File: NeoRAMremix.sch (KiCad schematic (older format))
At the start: 27 parts, among them P1 C64-Exp-Port, Q1 2N3904, SW1 Reset, U1 HM628512BFP-5, U2 HM628512BFP-5, U3 HM628512BFP-5, U4 HM628512BFP-5

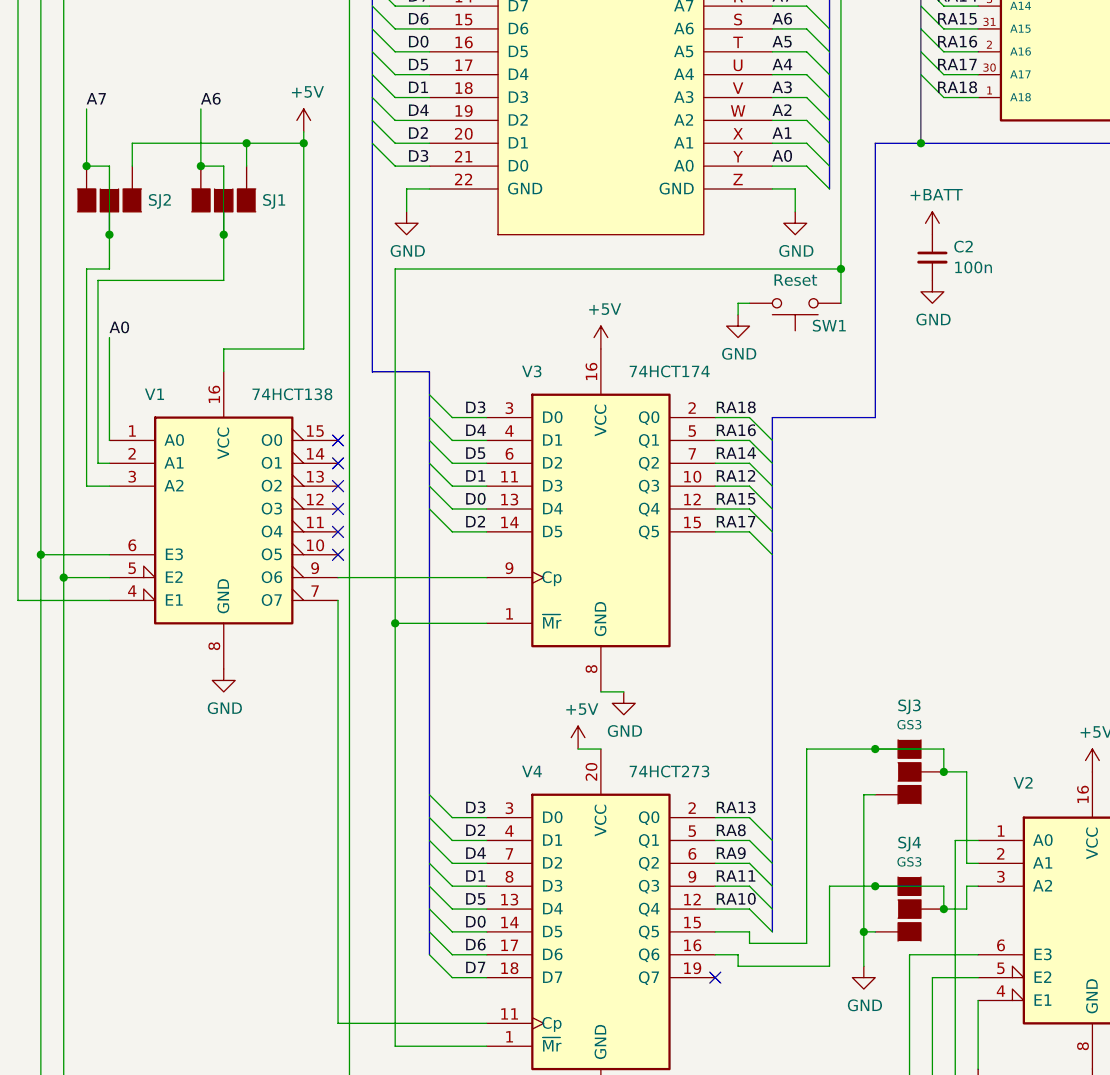
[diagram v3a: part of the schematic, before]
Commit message: Fixed solder bridges.
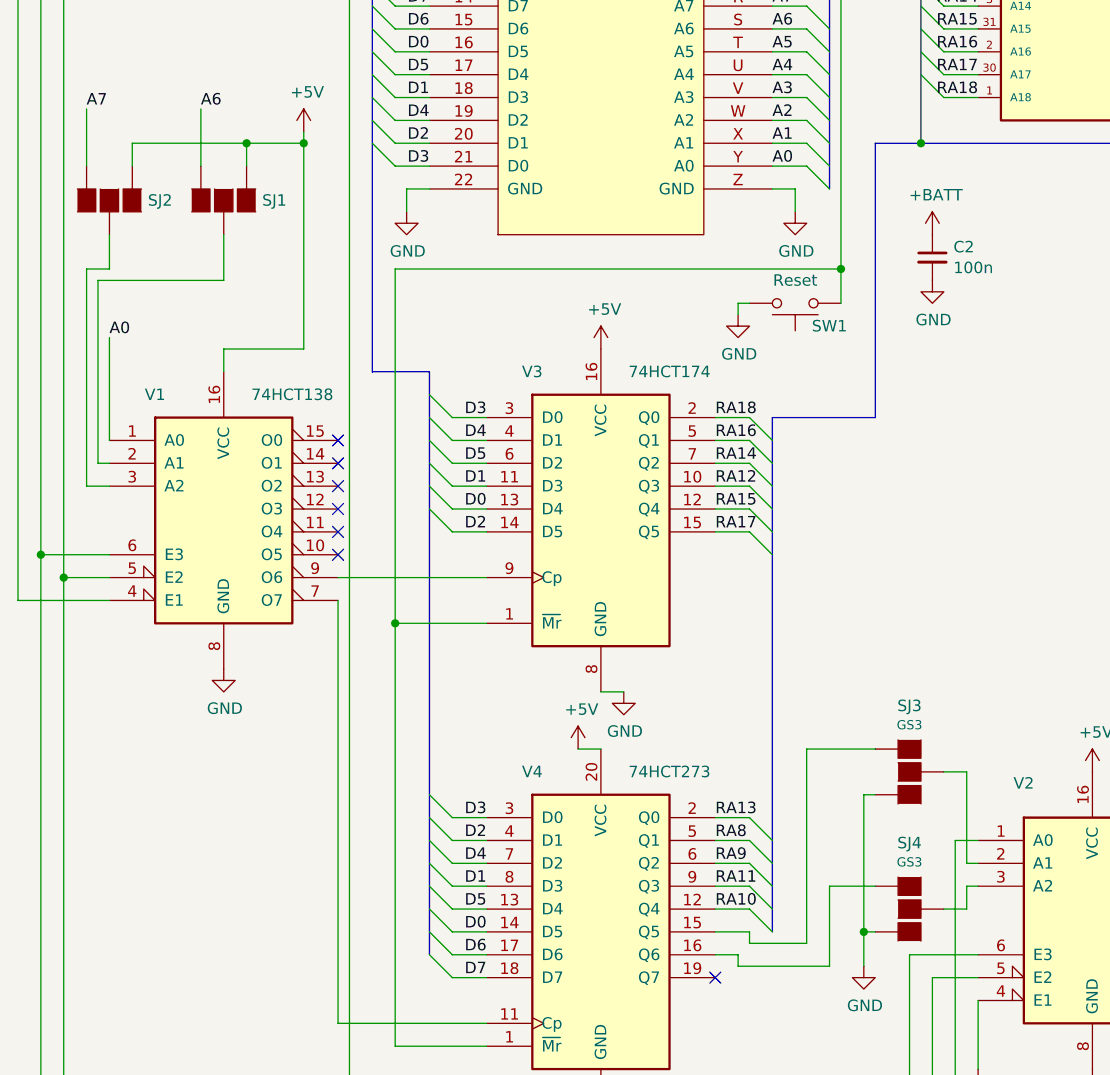
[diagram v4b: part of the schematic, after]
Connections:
- net A6: no longer SJ1.2 (G2), V1.2 (A1)
- net A7: no longer SJ2.2 (G2), V1.3 (A2)
- net at SJ3.1 (G1), V4.15 (Q5): no longer SJ3.2 (G2), V2.2 (A1)
- net at SJ4.1 (G1), V4.16 (Q6): no longer SJ4.2 (G2), V2.3 (A2)
- new net: SJ1.2 (G2), V1.2 (A1)
- new net: SJ2.2 (G2), V1.3 (A2)
- new net: SJ3.2 (G2), V2.2 (A1)
- new net: SJ4.2 (G2), V2.3 (A2)
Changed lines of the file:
@@
 	6150 3300 7850 3300
-Wire Wire Line
-	800  3400 900  3400
-Wire Wire Line
-	900  3400 900  3700
-Connection ~ 800  3400
-Connection ~ 900  3700
-Wire Wire Line
-	1300 3400 1400 3400
-Wire Wire Line
-	1400 3400 1400 3700
-Connection ~ 1300 3400
-Connection ~ 1400 3700
-Wire Wire Line
-	4250 5950 4550 5950
-Wire Wire Line
-	4550 5950 4550 6050
-Connection ~ 4250 5950
 Wire Wire Line
 	4700 6450 4650 6450
@@
 Wire Wire Line
 	4650 6050 4550 6050
-Connection ~ 4550 6050
 Wire Wire Line
 	4700 6550 4650 6550
@@
 Wire Wire Line
 	4650 6650 4550 6650
-Wire Wire Line
-	4250 6550 4550 6550
-Wire Wire Line
-	4550 6550 4550 6650
-Connection ~ 4250 6550
-Connection ~ 4550 6650
 $Comp
 L power:PWR_FLAG #FLG0103

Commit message: Fixed solder bridges.
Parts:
- removed SJ1, SJ2, SJ3, SJ4: GS3, Connectors:GS3, symbol NeoRAMremix-rescue:GS3-w_conn
- added SJ1, SJ2, SJ3, SJ4: SolderJumper_3_Bridged12, Jumper:SolderJumper-3_P1.3mm_Bridged12_RoundedPad1.0x1.5mm, symbol Jumper:SolderJumper_3_Bridged12
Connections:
- wire segments 302 -> 299
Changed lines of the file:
@@
 Wire Wire Line
 	4700 7050 4700 7350
-$Comp
-L NeoRAMremix-rescue:GS3-w_conn SJ3
-U 1 1 5C6A02C1
-P 4400 6050
-F 0 "SJ3" H 4400 6339 50  0000 C CNN
-F 1 "GS3" H 4400 6255 40  0000 C CNN
-F 2 "Connectors:GS3" H 4400 6050 50  0001 C CNN
-F 3 "" H 4400 6050 50  0001 C CNN
-	1    4400 6050
-	1    0    0    -1
-$EndComp
-$Comp
-L NeoRAMremix-rescue:GS3-w_conn SJ4
-U 1 1 5C6A0422
-P 4400 6650
-F 0 "SJ4" H 4400 6939 50  0000 C CNN
-F 1 "GS3" H 4400 6855 40  0000 C CNN
-F 2 "Connectors:GS3" H 4400 6650 50  0001 C CNN
-F 3 "" H 4400 6650 50  0001 C CNN
-	1    4400 6650
-	1    0    0    -1
-$EndComp
 NoConn ~ 3550 6950
 Wire Wire Line
@@
 	3700 6800 3950 6800
 Wire Wire Line
-	3950 6800 3950 5950
-Wire Wire Line
-	3950 5950 4250 5950
-Wire Wire Line
 	3550 6850 3650 6850
 Wire Wire Line
@@
 Wire Wire Line
 	3650 6900 4050 6900
-Wire Wire Line
-	4050 6900 4050 6550
-Wire Wire Line
-	4050 6550 4250 6550
-Wire Wire Line
-	4250 6150 4200 6150
-Wire Wire Line
-	4200 6150 4200 6750
-Wire Wire Line
-	4200 6750 4250 6750
 $Comp
 L power:GND #PWR0133
 U 1 1 5C7915DA
-P 4200 6900
-F 0 "#PWR0133" H 4200 6650 50  0001 C CNN
-F 1 "GND" H 4205 6727 50  0000 C CNN
-F 2 "" H 4200 6900 50  0001 C CNN
-F 3 "" H 4200 6900 50  0001 C CNN
-	1    4200 6900
-	1    0    0    -1
-$EndComp
-Wire Wire Line
-	4200 6750 4200 6900
-Connection ~ 4200 6750
-$Comp
-L NeoRAMremix-rescue:GS3-w_conn SJ1
-U 1 1 5C7D2316
-P 1400 3550
-F 0 "SJ1" V 1400 3718 50  0000 L CNN
-F 1 "GS3" V 1446 3718 40  0001 L CNN
-F 2 "Connectors:GS3" H 1400 3550 50  0001 C CNN
-F 3 "" H 1400 3550 50  0001 C CNN
-	1    1400 3550
-	0    1    1    0
-$EndComp
-$Comp
-L NeoRAMremix-rescue:GS3-w_conn SJ2
-U 1 1 5C7F2916
-P 900 3550
-F 0 "SJ2" V 900 3718 50  0000 L CNN
-F 1 "GS3" V 946 3718 40  0001 L CNN
-F 2 "Connectors:GS3" H 900 3550 50  0001 C CNN
-F 3 "" H 900 3550 50  0001 C CNN
-	1    900  3550
-	0    1    1    0
+P 4200 7000
+F 0 "#PWR0133" H 4200 6750 50  0001 C CNN
+F 1 "GND" H 4205 6827 50  0000 C CNN
+F 2 "" H 4200 7000 50  0001 C CNN
+F 3 "" H 4200 7000 50  0001 C CNN
+	1    4200 7000
+	1    0    0    -1
 $EndComp
 Wire Wire Line
@@
 Wire Wire Line
 	800  4800 800  3850
-Wire Wire Line
-	800  3850 900  3850
-Wire Wire Line
-	900  3850 900  3700
 $Comp
 L device:CP C1
@@
 D3
 Wire Wire Line
-	850  3900 1400 3900
-Wire Wire Line
-	1400 3900 1400 3700
-Wire Wire Line
 	850  3900 850  4700
 Wire Wire Line
 	1750 3250 1750 3300
 Wire Wire Line
-	1750 3300 1500 3300
-Wire Wire Line
-	1000 3300 1000 3400
-Wire Wire Line
-	1500 3400 1500 3300
-Connection ~ 1500 3300
-Wire Wire Line
-	1500 3300 1000 3300
-Wire Wire Line
 	1400 4300 1400 4200
 Wire Wire Line
 	1400 4200 1750 4200
 Wire Wire Line
-	1750 4200 1750 3300
+	1750 4200 1750 3550
 Connection ~ 1750 3300
-Wire Wire Line
-	800  3150 800  3400
-Wire Wire Line
-	1300 3150 1300 3400
 Text Label 6400 2100 2    50   ~ 0
 RA8
@@
 Wire Wire Line
 	4650 6050 4550 6050
-Wire Wire Line
-	4700 6550 4650 6550
-Wire Wire Line
-	4650 6550 4650 6650
-Wire Wire Line
-	4650 6650 4550 6650
 $Comp
 L power:PWR_FLAG #FLG0103
@@
 	1    0    0    -1
 $EndComp
-Text Label 1300 3150 0    50   ~ 0
+Text Label 1350 3150 0    50   ~ 0
 A6
 Text Label 800  3150 0    50   ~ 0
@@
 Wire Wire Line
 	3650 4000 3700 4000
+$Comp
+L Jumper:SolderJumper_3_Bridged12 SJ2
+U 1 1 5C5C59E5
+P 1000 3550
+F 0 "SJ2" H 1000 3664 50  0000 C CNN
+F 1 "SolderJumper_3_Bridged12" H 1000 3664 50  0001 C CNN
+F 2 "Jumper:SolderJumper-3_P1.3mm_Bridged12_RoundedPad1.0x1.5mm" H 1000 3550 50  0001 C CNN
+F 3 "~" H 1000 3550 50  0001 C CNN
+	1    1000 3550
+	1    0    0    -1
+$EndComp
+Wire Wire Line
+	800  3550 800  3150
+Wire Wire Line
+	1000 3850 1000 3700
+Wire Wire Line
+	800  3850 1000 3850
+Wire Wire Line
+	1200 3550 1200 3300
+$Comp
+L Jumper:SolderJumper_3_Bridged12 SJ1
+U 1 1 5C62F605
+P 1550 3550
+F 0 "SJ1" H 1550 3664 50  0000 C CNN
+F 1 "SolderJumper_3_Bridged12" H 1550 3664 50  0001 C CNN
+F 2 "Jumper:SolderJumper-3_P1.3mm_Bridged12_RoundedPad1.0x1.5mm" H 1550 3550 50  0001 C CNN
+F 3 "~" H 1550 3550 50  0001 C CNN
+	1    1550 3550
+	1    0    0    -1
+$EndComp
+Connection ~ 1750 3550
+Wire Wire Line
+	1750 3550 1750 3300
+Wire Wire Line
+	1200 3300 1750 3300
+Wire Wire Line
+	850  3900 1550 3900
+Wire Wire Line
+	1550 3900 1550 3700
+Wire Wire Line
+	1350 3550 1350 3150
+$Comp
+L Jumper:SolderJumper_3_Bridged12 SJ3
+U 1 1 5C6BABBB
+P 4400 6050
+F 0 "SJ3" V 4400 6118 50  0000 L CNN
+F 1 "SolderJumper_3_Bridged12" H 4400 6164 50  0001 C CNN
+F 2 "Jumper:SolderJumper-3_P1.3mm_Bridged12_RoundedPad1.0x1.5mm" H 4400 6050 50  0001 C CNN
+F 3 "~" H 4400 6050 50  0001 C CNN
+	1    4400 6050
+	0    -1   1    0
+$EndComp
+Wire Wire Line
+	3950 5850 4400 5850
+Wire Wire Line
+	3950 5850 3950 6800
+$Comp
+L Jumper:SolderJumper_3_Bridged12 SJ4
+U 1 1 5C7687C6
+P 4400 6550
+F 0 "SJ4" V 4400 6618 50  0000 L CNN
+F 1 "SolderJumper_3_Bridged12" H 4400 6664 50  0001 C CNN
+F 2 "Jumper:SolderJumper-3_P1.3mm_Bridged12_RoundedPad1.0x1.5mm" H 4400 6550 50  0001 C CNN
+F 3 "~" H 4400 6550 50  0001 C CNN
+	1    4400 6550
+	0    -1   1    0
+$EndComp
+Wire Wire Line
+	4700 6550 4550 6550
+Wire Wire Line
+	4050 6350 4400 6350
+Wire Wire Line
+	4050 6350 4050 6900
+Wire Wire Line
+	4200 6750 4200 7000
+Wire Wire Line
+	4200 6750 4400 6750
+Wire Wire Line
+	4200 6750 4200 6250
+Wire Wire Line
+	4200 6250 4400 6250
 Wire Bus Line
 	6150 2000 6150 3300
@@
 Wire Bus Line
 	2300 4300 2300 6850
+Connection ~ 4200 6750
 $EndSCHEMATC

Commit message: Fixing RAM footprint.
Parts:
- U4: footprint Housings_SSOP:TSOP-II-32_21.0x10.2mm_Pitch1.27mm -> NeoRAMremix:SO32_FP32D_20.45x11.3mm_Pitch1.27mm
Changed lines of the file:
@@
 F 0 "U4" H 10300 3100 50  0000 C CNN
 F 1 "HM628512BFP-5" H 9900 3250 50  0000 C CNN
-F 2 "Housings_SSOP:TSOP-II-32_21.0x10.2mm_Pitch1.27mm" H 10300 2200 50  0001 C CIN
+F 2 "NeoRAMremix:SO32_FP32D_20.45x11.3mm_Pitch1.27mm" H 10300 2200 50  0001 C CIN
 F 3 "" H 10300 2200 50  0001 C CNN
 	1    10300 2200
@@
 Wire Wire Line
 	4200 6250 4400 6250
+Connection ~ 4200 6750
 Wire Bus Line
 	6150 2000 6150 3300
@@
 Wire Bus Line
 	2300 4300 2300 6850
-Connection ~ 4200 6750
 $EndSCHEMATC

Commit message: Fixing RAM footprint.
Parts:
- U1, U2, U3: footprint Housings_SSOP:TSOP-II-32_21.0x10.2mm_Pitch1.27mm -> NeoRAMremix:SO32_FP32D_20.45x11.3mm_Pitch1.27mm
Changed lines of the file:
@@
 F 0 "U1" H 5200 3100 50  0000 C CNN
 F 1 "HM628512BFP-5" H 4800 3250 50  0000 C CNN
-F 2 "Housings_SSOP:TSOP-II-32_21.0x10.2mm_Pitch1.27mm" H 5200 2200 50  0001 C CIN
+F 2 "NeoRAMremix:SO32_FP32D_20.45x11.3mm_Pitch1.27mm" H 5200 2200 50  0001 C CIN
 F 3 "" H 5200 2200 50  0001 C CNN
 	1    5200 2200
@@
 F 0 "U2" H 6900 3100 50  0000 C CNN
 F 1 "HM628512BFP-5" H 6500 3250 50  0000 C CNN
-F 2 "Housings_SSOP:TSOP-II-32_21.0x10.2mm_Pitch1.27mm" H 6900 2200 50  0001 C CIN
+F 2 "NeoRAMremix:SO32_FP32D_20.45x11.3mm_Pitch1.27mm" H 6900 2200 50  0001 C CIN
 F 3 "" H 6900 2200 50  0001 C CNN
 	1    6900 2200
@@
 F 0 "U3" H 8600 3100 50  0000 C CNN
 F 1 "HM628512BFP-5" H 8200 3250 50  0000 C CNN
-F 2 "Housings_SSOP:TSOP-II-32_21.0x10.2mm_Pitch1.27mm" H 8600 2200 50  0001 C CIN
+F 2 "NeoRAMremix:SO32_FP32D_20.45x11.3mm_Pitch1.27mm" H 8600 2200 50  0001 C CIN
 F 3 "" H 8600 2200 50  0001 C CNN
 	1    8600 2200
